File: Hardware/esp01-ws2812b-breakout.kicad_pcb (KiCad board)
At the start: 2 copper layers, 17 parts, among them J1 Screw_Terminal_01x02, J2 Screw_Terminal_01x04, J3 Conn_01x03_Male, Q1 IRFS4127, Q2 IRFS4127, U1 LM1117-3.3, U2 ESP-01v090, U3 DS18B20

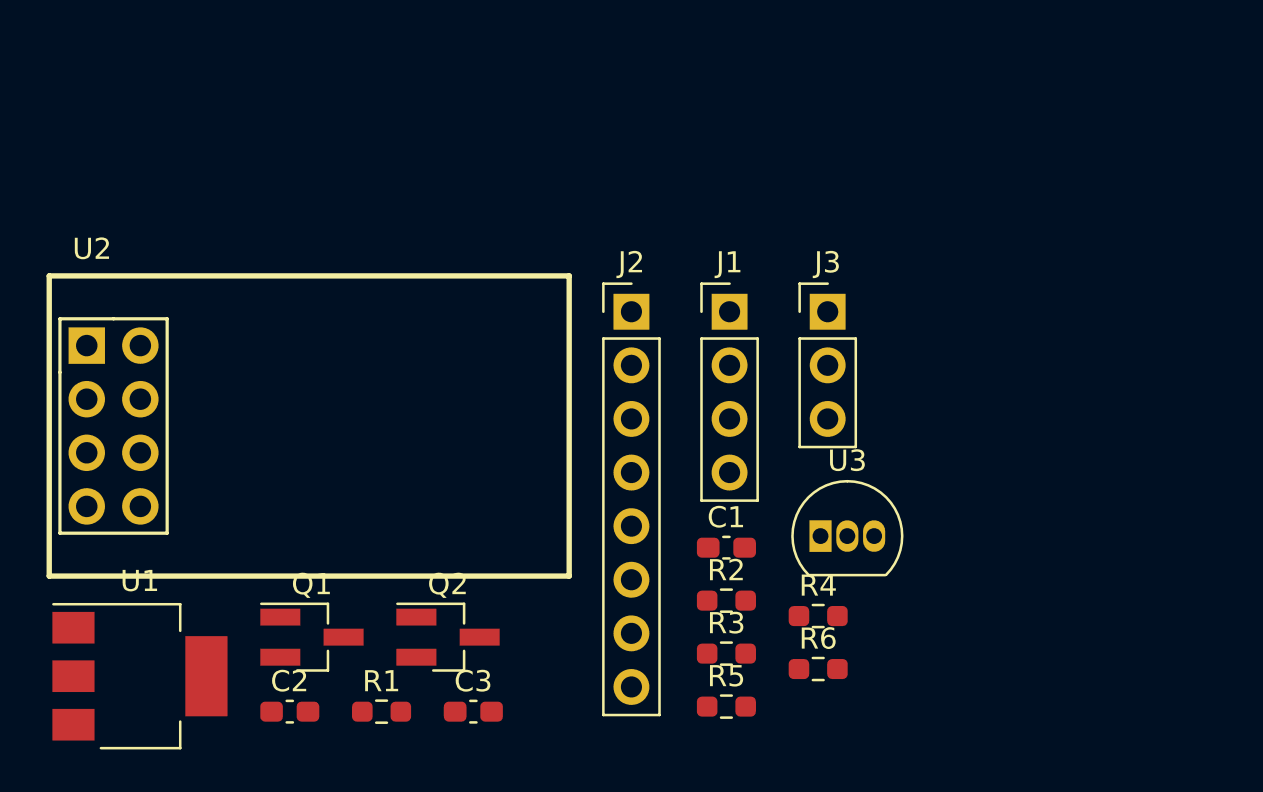
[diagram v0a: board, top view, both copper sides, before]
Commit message: Finished PCB layout
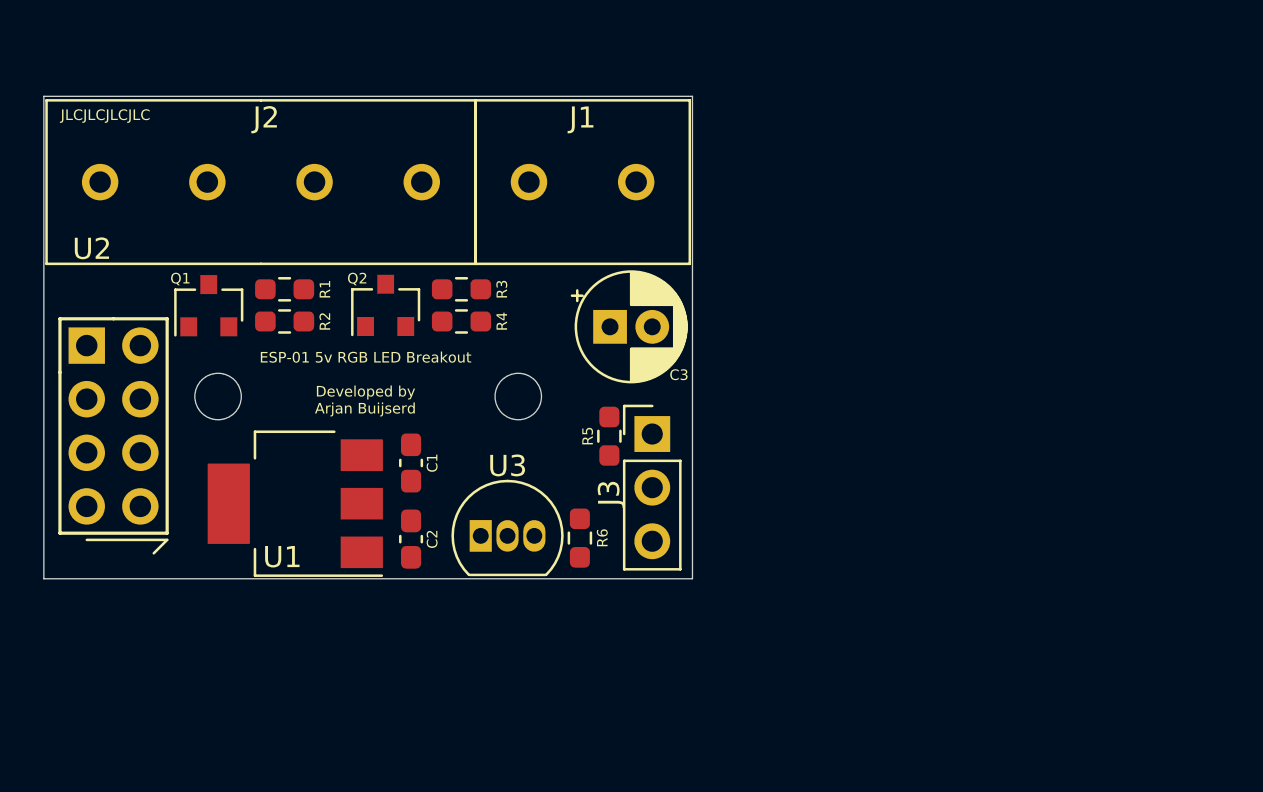
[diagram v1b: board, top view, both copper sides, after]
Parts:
- added H1: MountingHole, MountingHole:MountingHole_2.2mm_M2, F.Cu at (135.1, 96.0)
- added H2: MountingHole, MountingHole:MountingHole_2.2mm_M2, F.Cu at (149.4, 96.0)
- C3: footprint Capacitor_SMD:C_0603_1608Metric_Pad1.08x0.95mm_HandSolder -> Capacitor_THT:CP_Radial_D5.0mm_P2.00mm
- J1: footprint Connector_PinHeader_2.54mm:PinHeader_1x04_P2.54mm_Vertical -> Custom Terminals:0102-blue-terminal
- J2: footprint Connector_PinHeader_2.54mm:PinHeader_1x08_P2.54mm_Vertical -> Custom Terminals:0104-blue-terminal
- Q1, Q2: footprint ESP8266:SOT-23_Handsoldering_DS-REVERSED -> Custom Mosfets:SOT-23_DS-REVERSED
- moved R2 24.8 mm to (138.3, 92.5)
- moved R4 21.9 mm to (146.7, 92.5)
- moved R3 21.3 mm to (146.7, 90.9)
- moved R1 20.5 mm to (138.3, 90.9)
- moved C3 19.4 mm to (153.7, 92.7)
- moved Q1 16.4 mm to (134.7, 91.7), turned to 90 degrees
- moved U3 16.1 mm to (147.6, 102.6)
- moved Q2 16.0 mm to (143.1, 91.7), turned to 90 degrees
- moved C1 15.5 mm to (144.3, 99.2), turned to 270 degrees
- moved R5 14.0 mm to (153.7, 97.9), turned to 90 degrees
- moved R6 12.9 mm to (152.3, 102.7), turned to 90 degrees
- moved J2 11.7 mm to (144.8, 85.9), turned to 180 degrees
- moved U1 11.0 mm to (138.8, 101.1), turned to 180 degrees
- moved J3 10.1 mm to (155.7, 97.8)
- moved C2 9.99 mm to (144.3, 102.8), turned to 270 degrees
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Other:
- board outline added: 30.7 x 22.9 mm
- board text added: "ESP-01 5v RGB LED Breakout Developed by Arjan Buijserd"
- board text added: "JLCJLCJLCJLC"

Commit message: Resistor footprints were still 0603, fixed now.
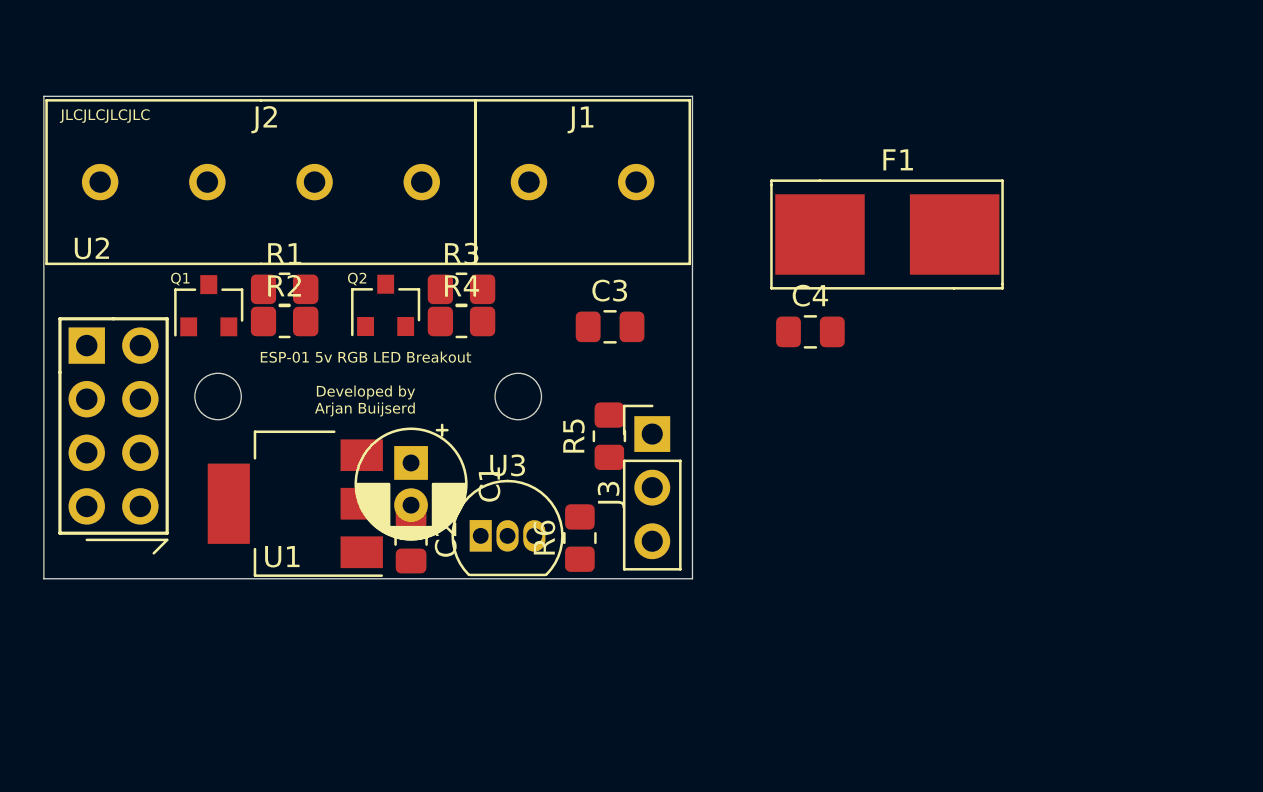
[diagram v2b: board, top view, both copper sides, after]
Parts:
- added C4: 1uF, Capacitor_SMD:C_0805_2012Metric_Pad1.18x1.45mm_HandSolder, F.Cu at (163.2, 93.0)
- added F1: 15A, Custom Fuses:1808_SMD_Fuse_Holder, F.Cu at (163.7, 88.3)
- C1: value 10uF -> 100uF; footprint Capacitor_SMD:C_0603_1608Metric_Pad1.08x0.95mm_HandSolder -> Capacitor_THT:CP_Radial_D5.0mm_P2.00mm
- C2: footprint Capacitor_SMD:C_0603_1608Metric_Pad1.08x0.95mm_HandSolder -> Capacitor_SMD:C_0805_2012Metric_Pad1.18x1.45mm_HandSolder
- C3: value 100uF -> 10uF; footprint Capacitor_THT:CP_Radial_D5.0mm_P2.00mm -> Capacitor_SMD:C_0805_2012Metric_Pad1.18x1.45mm_HandSolder
- R1, R2, R3, R4, R5, R6: footprint Resistor_SMD:R_0603_1608Metric_Pad0.98x0.95mm_HandSolder -> Resistor_SMD:R_0805_2012Metric_Pad1.20x1.40mm_HandSolder
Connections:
- C2 pad 1: +3V3 -> +5V
- C3 pad 1: +5V -> +3V3
- J1 pad 2: +5V -> Net-(F1-Pad2)

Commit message: Antenna clearance, redid layout
Some sources comment that the ESP8266's WiFi range can be extended dramatically by having the antenna 'sticking' out from the PCB. So I decided to inplement that. Additionally, the new footprints required me to redo the entire layout.
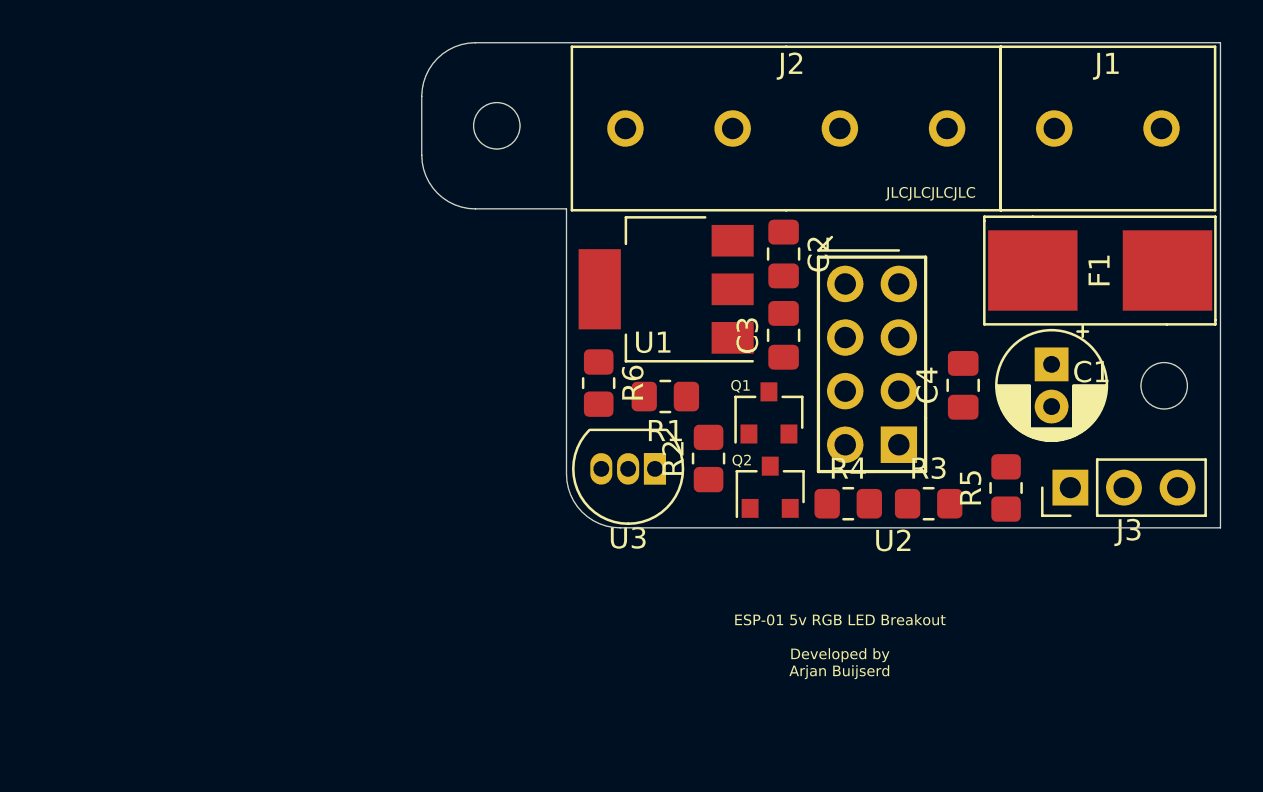
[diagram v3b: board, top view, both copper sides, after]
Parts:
- moved U2 38.8 mm to (167.4, 98.3), turned to 180 degrees
- moved C1 30.7 mm to (174.6, 94.5)
- moved H2 30.6 mm to (180.0, 95.5)
- moved Q1 27.0 mm to (161.2, 96.8)
- moved J1 25.0 mm to (179.8, 83.3)
- moved J2 25.0 mm to (169.7, 83.3)
- moved R3 24.4 mm to (168.8, 101.1)
- moved C2 22.2 mm to (161.9, 89.3)
- moved R2 21.1 mm to (158.4, 98.9), turned to 90 degrees
- moved U1 20.3 mm to (156.4, 90.9)
- moved R4 20.3 mm to (165.0, 101.1)
- moved Q2 20.2 mm to (161.3, 100.3)
- moved J3 20.0 mm to (175.5, 100.3), turned to 90 degrees
- moved R5 19.0 mm to (172.5, 100.3)
- moved R1 18.7 mm to (156.3, 96.0), turned to 180 degrees
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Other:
- board size 30.7 x 22.9 mm -> 37.8 x 23 mm

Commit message: Layout updates
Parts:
- moved R1 1.05 mm to (157.4, 96.0)
- moved R6 0.13 mm to (153.0, 95.4)
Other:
- board text added: "ESP-01 5V RGB LED Breakout Developed by Arjan Buijserd"
- board text removed: "ESP-01 5v RGB LED Breakout Developed by Arjan Buijserd"

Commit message: Started routing
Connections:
- J3 pad 2: +3V3 -> GPIO0
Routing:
- net GPIO0: track 0.00 -> 21.7 mm, vias 0 -> 1
- net LED2_3V3: track 0.00 -> 21.0 mm, vias 0 -> 2
- net +3V3: track 0.00 -> 15.1 mm
- net +5V: track 0.00 -> 13.2 mm
- net GND: track 0.00 -> 11.6 mm
- added copper zone on F.Cu, net GND

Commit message: Continued routing
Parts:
- moved C4 0.38 mm to (170.4, 95.9)
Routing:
- net +3V3: track 15.1 -> 85.8 mm, vias 0 -> 2
- net +5V: track 13.2 -> 46.4 mm, vias 0 -> 3
- net LED2_5V: track 0.00 -> 23.9 mm, vias 0 -> 2
- net LED1_5V: track 0.00 -> 19.0 mm, vias 0 -> 1
- net GND: track 11.6 -> 27.9 mm, vias 0 -> 4
- net Net-(F1-Pad2): track 0.00 -> 8.95 mm
- net DALLAS: track 0.00 -> 7.25 mm
- net LED1_3V3: track 0.00 -> 6.23 mm, vias 0 -> 1
- net LED2_3V3: track 21.0 -> 22.3 mm
- net GPIO0: track 21.7 -> 22.1 mm, vias 1 -> 3

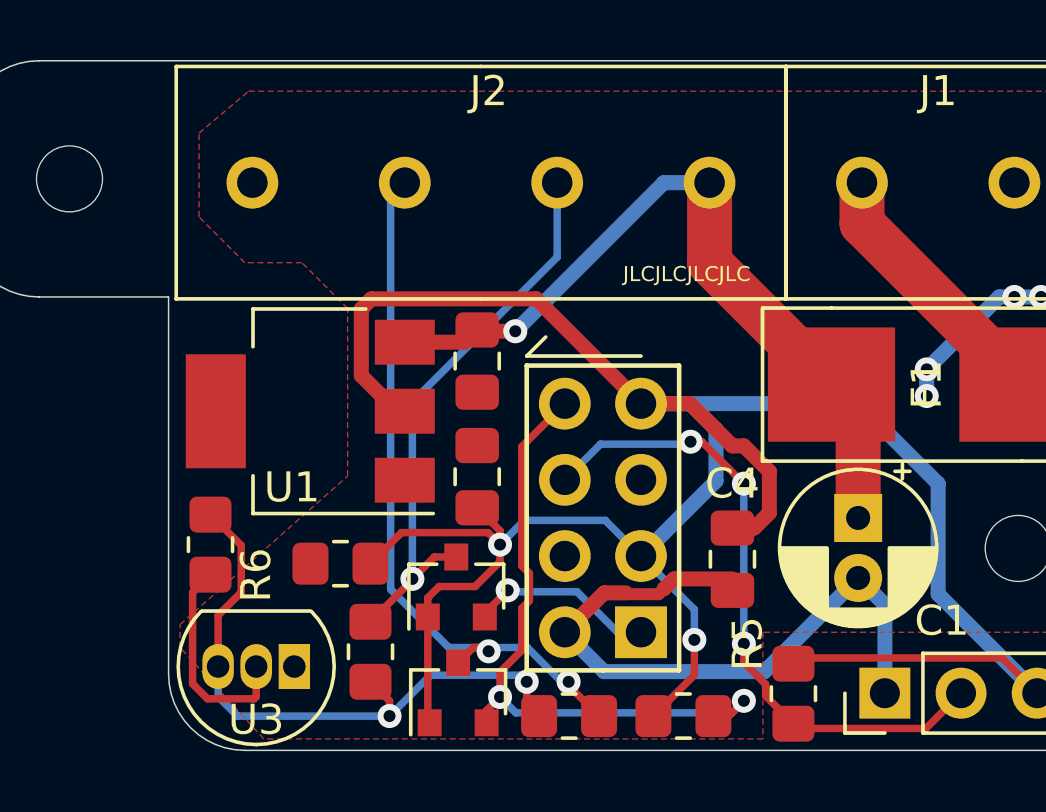
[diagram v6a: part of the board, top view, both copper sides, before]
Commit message: Finished PCB routing
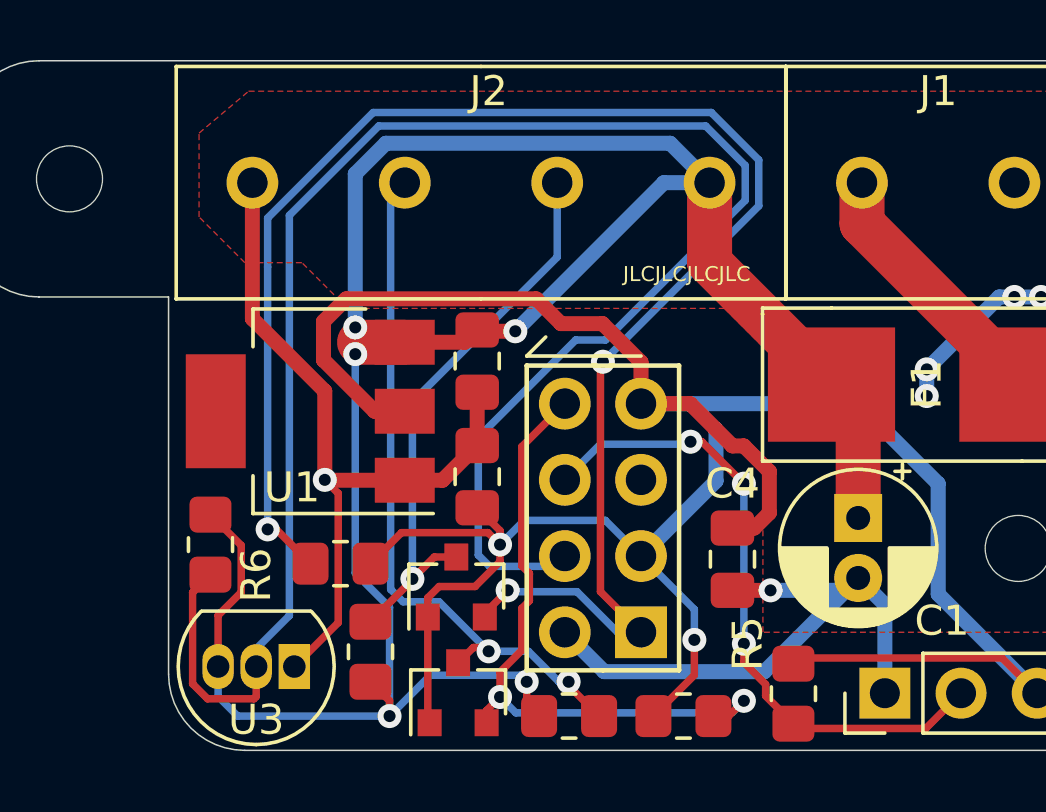
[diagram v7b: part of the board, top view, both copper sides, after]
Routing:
- net DALLAS: track 7.25 -> 60.2 mm
- net LED1_3V3: track 6.23 -> 55.5 mm, vias 1 -> 3
- net +5V: track 46.4 -> 79.4 mm, vias 3 -> 5
- net GND: track 27.9 -> 52.5 mm, vias 4 -> 6
- net +3V3: track 85.8 -> 88.9 mm
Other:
- board text added: "5V"
- board text added: "ESP-01 5V Addressable RGB LED Breakout Developed by Arjan Buijserd"
- board text added: "GND"
- board text added: "IN"
- board text added: "LED1"
- board text added: "LED2"
- board text added: "OUT"
- board text removed: "ESP-01 5V RGB LED Breakout Developed by Arjan Buijserd"

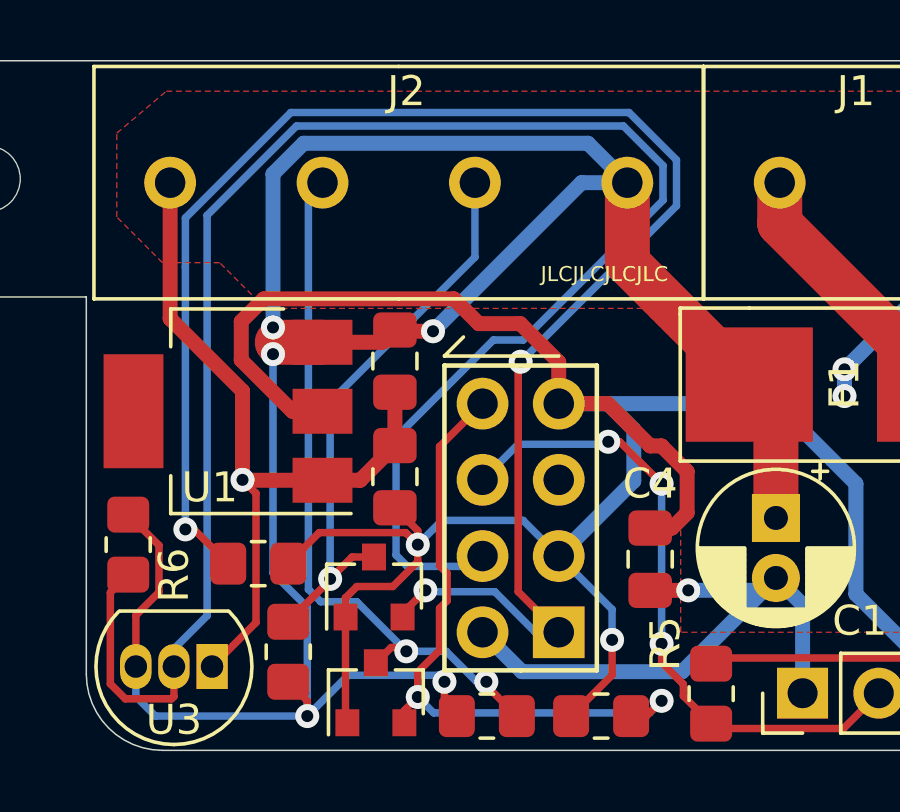
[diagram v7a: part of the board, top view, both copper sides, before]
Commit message: Finalized PCB layout, added PDF+PNG
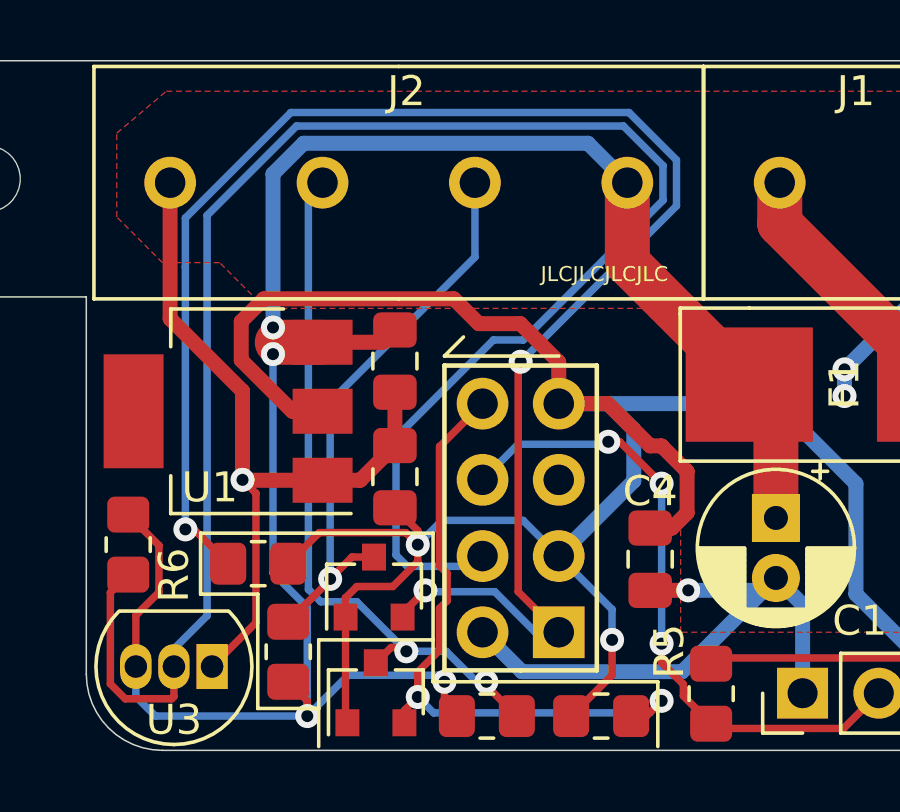
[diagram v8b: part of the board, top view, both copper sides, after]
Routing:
- net +5V: track 79.4 -> 69.6 mm, vias 5 -> 4
